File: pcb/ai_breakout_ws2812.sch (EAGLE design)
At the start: 4 parts, among them J1 1X03, J2 1X03

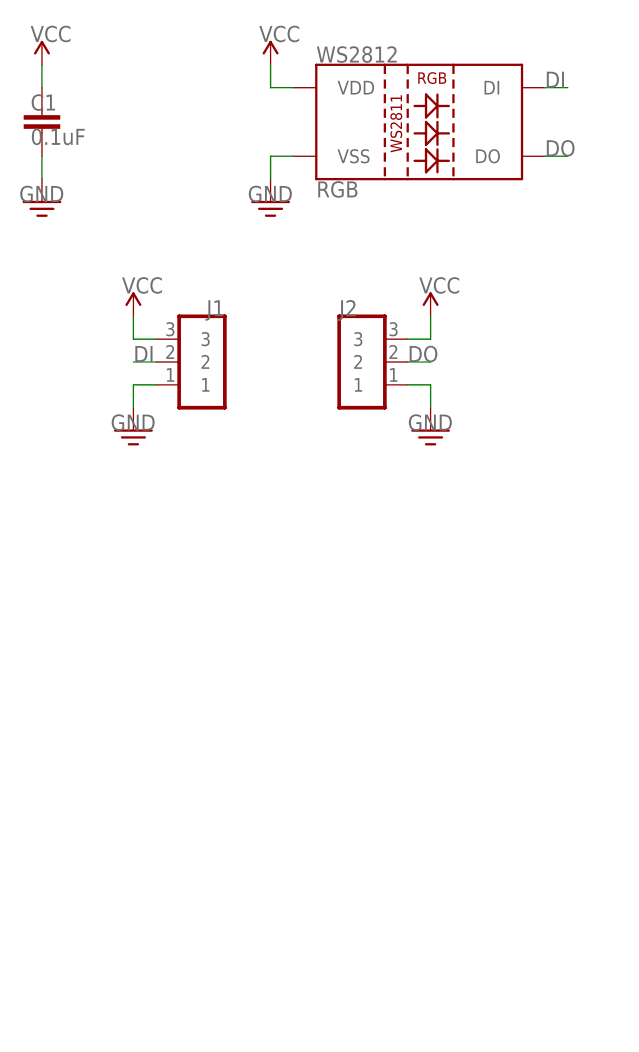
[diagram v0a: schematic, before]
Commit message: Corrected silkscreen widths, BOM, searchable PDF schematic.
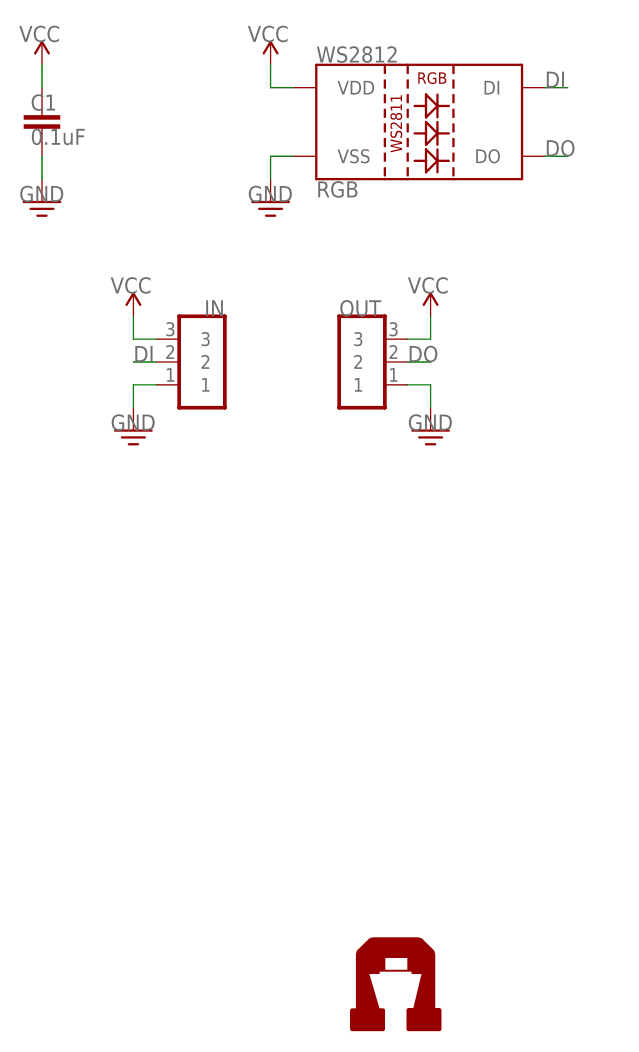
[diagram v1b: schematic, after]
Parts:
- added U$5: AI-LOGOL, Ai_Miscellany:AI-LOGOL
- renumbered J1 to IN, J2 to OUT
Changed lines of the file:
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@@
 <?xml version="1.0" encoding="utf-8"?>
 <!DOCTYPE eagle SYSTEM "eagle.dtd">
-<eagle version="6.4">
+<eagle version="6.5.0">
 <drawing>
 <settings>
-<setting alwaysvectorfont="yes"/>
+<setting alwaysvectorfont="no"/>
 <setting verticaltext="up"/>
 </settings>
-<grid distance="50" unitdist="mil" unit="mil" style="lines" multiple="1" display="yes" altdistance="0.01" altunitdist="inch" altunit="inch"/>
+<grid distance="0.1" unitdist="inch" unit="inch" style="lines" multiple="1" display="no" altdistance="0.01" altunitdist="inch" altunit="inch"/>
 <layers>
 <layer number="1" name="Top" color="4" fill="1" visible="no" active="no"/>
@@
 <part name="GND2" library="Ai_Power" deviceset="GND" device=""/>
 <part name="U$2" library="Ai_Power" deviceset="VCC" device=""/>
-<part name="J1" library="Ai_Connectors" deviceset="1X03" device=""/>
-<part name="J2" library="Ai_Connectors" deviceset="1X03" device=""/>
+<part name="IN" library="Ai_Connectors" deviceset="1X03" device=""/>
+<part name="OUT" library="Ai_Connectors" deviceset="1X03" device=""/>
 <part name="GND3" library="Ai_Power" deviceset="GND" device=""/>
 <part name="GND4" library="Ai_Power" deviceset="GND" device=""/>
 <part name="U$3" library="Ai_Power" deviceset="VCC" device=""/>
 <part name="U$4" library="Ai_Power" deviceset="VCC" device=""/>
+<part name="U$5" library="Ai_Miscellany" deviceset="AI-LOGO" device="L"/>
 </parts>
 <sheets>
@@
 <instance part="GND2" gate="GND" x="125.73" y="97.79"/>
 <instance part="U$2" gate="1" x="125.73" y="113.03"/>
-<instance part="J1" gate="G$1" x="118.11" y="80.01" rot="MR0"/>
-<instance part="J2" gate="G$1" x="135.89" y="80.01"/>
+<instance part="IN" gate="G$1" x="118.11" y="80.01" rot="MR0"/>
+<instance part="OUT" gate="G$1" x="135.89" y="80.01"/>
 <instance part="GND3" gate="GND" x="110.49" y="72.39"/>
 <instance part="GND4" gate="GND" x="143.51" y="72.39"/>
 <instance part="U$3" gate="1" x="110.49" y="85.09"/>
 <instance part="U$4" gate="1" x="143.51" y="85.09"/>
+<instance part="U$5" gate="G$1" x="139.7" y="10.16"/>
 </instances>
 <busses>
@@
 </segment>
 <segment>
-<pinref part="J2" gate="G$1" pin="3"/>
+<pinref part="OUT" gate="G$1" pin="3"/>
 <wire x1="140.97" y1="82.55" x2="143.51" y2="82.55" width="0.1524" layer="91"/>
 <pinref part="U$4" gate="1" pin="VCC"/>
@@
 </segment>
 <segment>
-<pinref part="J1" gate="G$1" pin="3"/>
+<pinref part="IN" gate="G$1" pin="3"/>
 <wire x1="113.03" y1="82.55" x2="110.49" y2="82.55" width="0.1524" layer="91"/>
 <pinref part="U$3" gate="1" pin="VCC"/>
@@
 </segment>
 <segment>
-<pinref part="J2" gate="G$1" pin="1"/>
+<pinref part="OUT" gate="G$1" pin="1"/>
 <wire x1="140.97" y1="77.47" x2="143.51" y2="77.47" width="0.1524" layer="91"/>
 <pinref part="GND4" gate="GND" pin="GND"/>
@@
 </segment>
 <segment>
-<pinref part="J1" gate="G$1" pin="1"/>
+<pinref part="IN" gate="G$1" pin="1"/>
 <wire x1="113.03" y1="77.47" x2="110.49" y2="77.47" width="0.1524" layer="91"/>
 <pinref part="GND3" gate="GND" pin="GND"/>
@@
 </segment>
 <segment>
-<pinref part="J1" gate="G$1" pin="2"/>
+<pinref part="IN" gate="G$1" pin="2"/>
 <wire x1="113.03" y1="80.01" x2="110.49" y2="80.01" width="0.1524" layer="91"/>
 <label x="110.49" y="80.01" size="1.778" layer="95"/>
@@
 </segment>
 <segment>
-<pinref part="J2" gate="G$1" pin="2"/>
+<pinref part="OUT" gate="G$1" pin="2"/>
 <wire x1="140.97" y1="80.01" x2="143.51" y2="80.01" width="0.1524" layer="91"/>
 <label x="140.97" y="80.01" size="1.778" layer="95"/>

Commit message: Minor modifications.  Version is now 1.1.
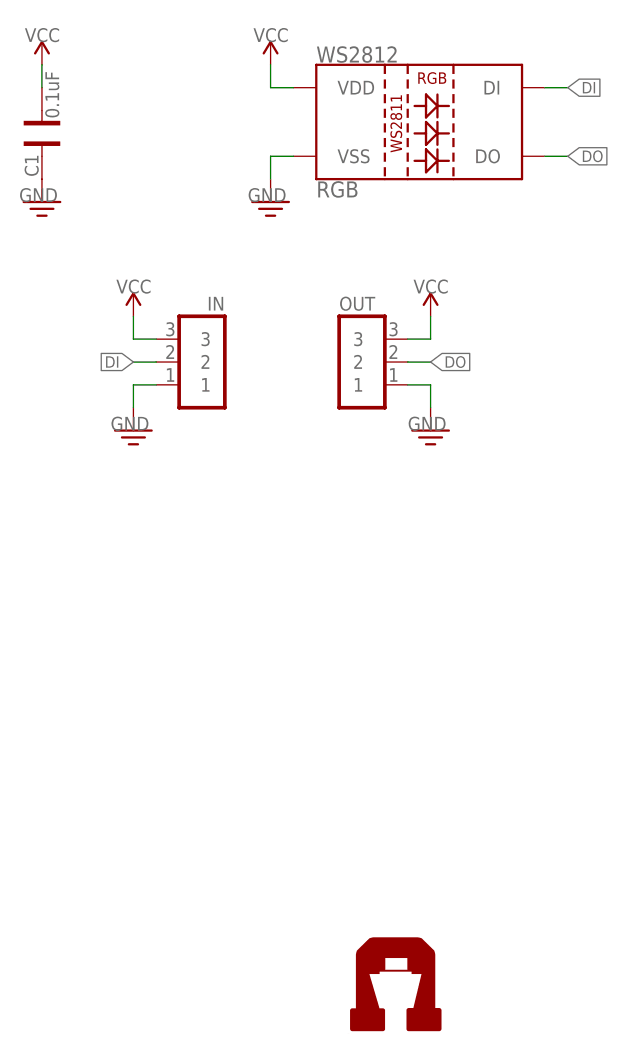
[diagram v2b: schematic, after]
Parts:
- C1: device Ai_Passives:CAP -> Ai_Passives:CAP0603
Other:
- moved on the sheet: C1
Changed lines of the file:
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@@
 <setting verticaltext="up"/>
 </settings>
-<grid distance="0.1" unitdist="inch" unit="inch" style="lines" multiple="1" display="no" altdistance="0.01" altunitdist="inch" altunit="inch"/>
+<grid distance="25" unitdist="mil" unit="mil" style="lines" multiple="1" display="yes" altdistance="0.01" altunitdist="inch" altunit="inch"/>
 <layers>
 <layer number="1" name="Top" color="4" fill="1" visible="no" active="no"/>
@@
 <part name="FRAME1" library="Ai_Miscellany" deviceset="FRAME-LETTER" device="">
 <attribute name="AUTHOR" value="A.I. HARDWARE SITH LORDS"/>
-<attribute name="REV" value="1.0"/>
+<attribute name="REV" value="1.1"/>
 </part>
 <part name="RGB" library="Ai_LED" deviceset="LED-WS2812" device=""/>
-<part name="C1" library="Ai_Passives" deviceset="CAP" device="" value="0.1uF"/>
+<part name="C1" library="Ai_Passives" deviceset="CAP" device="0603" value="0.1uF"/>
 <part name="U$1" library="Ai_Power" deviceset="VCC" device=""/>
 <part name="GND1" library="Ai_Power" deviceset="GND" device=""/>
@@
 <segment>
 <pinref part="C1" gate="G$1" pin="2"/>
-<wire x1="100.33" y1="102.87" x2="100.33" y2="100.33" width="0.1524" layer="91"/>
 <pinref part="GND1" gate="GND" pin="GND"/>
 </segment>
@@
 <pinref part="RGB" gate="U1" pin="DI"/>
 <wire x1="156.21" y1="110.49" x2="158.75" y2="110.49" width="0.1524" layer="91"/>
-<label x="156.21" y="110.49" size="1.778" layer="95"/>
+<label x="158.75" y="110.49" size="1.27" layer="95" ratio="15" xref="yes"/>
 </segment>
 <segment>
 <pinref part="IN" gate="G$1" pin="2"/>
 <wire x1="113.03" y1="80.01" x2="110.49" y2="80.01" width="0.1524" layer="91"/>
-<label x="110.49" y="80.01" size="1.778" layer="95"/>
+<label x="110.49" y="80.01" size="1.27" layer="95" ratio="15" rot="R180" xref="yes"/>
 </segment>
 </net>
@@
 <pinref part="RGB" gate="U1" pin="DO"/>
 <wire x1="156.21" y1="102.87" x2="158.75" y2="102.87" width="0.1524" layer="91"/>
-<label x="156.21" y="102.87" size="1.778" layer="95"/>
+<label x="158.75" y="102.87" size="1.27" layer="95" ratio="15" xref="yes"/>
 </segment>
 <segment>
 <pinref part="OUT" gate="G$1" pin="2"/>
 <wire x1="140.97" y1="80.01" x2="143.51" y2="80.01" width="0.1524" layer="91"/>
-<label x="140.97" y="80.01" size="1.778" layer="95"/>
-</segment>
-</net>
+<label x="143.51" y="80.01" size="1.27" layer="95" ratio="15" xref="yes"/>
+</segment>
+</net>
